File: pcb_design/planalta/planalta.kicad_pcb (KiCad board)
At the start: 2 copper layers, 93 x 93 mm, 158 parts, among them J1 USB_C_Receptacle, J2 USB_C_Receptacle, J3 USB_C_Receptacle, J4 USB_C_Receptacle, J5 Conn_02x13_Odd_Even, J6 Conn_02x03_Counter_Clockwise, J9 Conn_01x06_Female, Q1 Q_NMOS_GSD, Q2 Q_NMOS_GSD, Q3 Q_NMOS_GSD, Q4 Q_NMOS_GSD, Q5 Q_NMOS_GSD, SW1 SW_Push, U1 MAX4475_var, U10 dsPIC33EP512MC806, U11 DG2034E, U12 LP2985-5.0, U13 REF2033, U14 OPA320, U15 PGA113, U16 PGA113, U17 TPS737, U18 SiP32431, U19 SiP32431, U2 MAX4475_var, U20 SiP32431, U21 DG2034E, U22 DG2034E, U23 DG2034E, U24 SiP32431, U25 SiP32431, U3 MAX4475_var, U4 MAX4475_var, U5 PGA113, U6 PGA113, U7 MCP2542FD, U8 ADM7170, U9 ADS8332, Y1 Crystal_GND24

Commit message: Update.
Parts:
- moved D1 103.6 mm to (56.3, 129.4), turned to 90 degrees
- moved R17 98.4 mm to (56.3, 126.2), turned to 90 degrees
- moved D2 85.9 mm to (113.7, 129.4), turned to 90 degrees
- moved R18 79.6 mm to (113.7, 126.3), turned to 90 degrees
- moved C3 10.6 mm to (99.4, 48.4)
- moved R4 10.0 mm to (96.3, 48.4)
- moved Q3 9.94 mm to (92.7, 49.3)
- moved C36 9.09 mm to (58.7, 64.6)
- moved U18 9.09 mm to (58.7, 67.1)
- moved U7 8.74 mm to (92.3, 54.9)
- moved R3 7.16 mm to (95.9, 50.8), turned to -90 degrees
- moved C29 4.73 mm to (113.4, 80.6), turned to 0 degrees
- moved C20 3.37 mm to (100.0, 60.4)
- moved C19 3.30 mm to (97.5, 61.0)
- moved R33 3.13 mm to (89.2, 48.3), turned to 0 degrees
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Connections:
- net +3V3 renamed +3.3V
- J1 pad A10: /VMID -> /SCL1
- J1 pad A11: /CIN1 -> unconnected-(J1-PadA11)
- J1 pad A3: /OUT1 -> /SDA1
- J1 pad A6: /SDA1 -> /OUT1
- J1 pad A7: /SCL1 -> /CIN1
- J1 pad A8: unconnected-(J1-PadA8) -> /VMID
- J1 pad B10: /VMID -> /SCL1
- J1 pad B11: /CIN1 -> unconnected-(J1-PadB11)
- J1 pad B3: /OUT1 -> /SDA1
- J1 pad B6: /SDA1 -> /OUT1
- J1 pad B7: /SCL1 -> /CIN1
- J1 pad B8: unconnected-(J1-PadB8) -> /VMID
- J2 pad A10: /VMID -> /SCL1
- J2 pad A11: /CIN2 -> unconnected-(J2-PadA11)
- J2 pad A3: /OUT2 -> /SDA1
- J2 pad A6: /SDA1 -> /OUT2
- J2 pad A7: /SCL1 -> /CIN2
- J2 pad A8: unconnected-(J2-PadA8) -> /VMID
- J2 pad B10: /VMID -> /SCL1
- J2 pad B11: /CIN2 -> unconnected-(J2-PadB11)
- J2 pad B3: /OUT2 -> /SDA1
- J2 pad B6: /SDA1 -> /OUT2
- J2 pad B7: /SCL1 -> /CIN2
- J2 pad B8: unconnected-(J2-PadB8) -> /VMID
- J3 pad A10: /VMID -> /SCL2
- J3 pad A11: /CIN3 -> unconnected-(J3-PadA11)
- J3 pad A3: /OUT3 -> /SDA2
- J3 pad A6: /SDA2 -> /OUT3
- J3 pad A7: /SCL2 -> /CIN3
- J3 pad A8: unconnected-(J3-PadA8) -> /VMID
- J3 pad B10: /VMID -> /SCL2
- J3 pad B11: /CIN3 -> unconnected-(J3-PadB11)
- J3 pad B3: /OUT3 -> /SDA2
- J3 pad B6: /SDA2 -> /OUT3
- J3 pad B7: /SCL2 -> /CIN3
- J3 pad B8: unconnected-(J3-PadB8) -> /VMID
- J4 pad A10: /VMID -> /SCL2
- J4 pad A11: /CIN4 -> unconnected-(J4-PadA11)
- J4 pad A3: /OUT4 -> /SDA2
- J4 pad A6: /SDA2 -> /OUT4
- J4 pad A7: /SCL2 -> /CIN4
- J4 pad A8: unconnected-(J4-PadA8) -> /VMID
- J4 pad B10: /VMID -> /SCL2
- J4 pad B11: /CIN4 -> unconnected-(J4-PadB11)
- J4 pad B3: /OUT4 -> /SDA2
- J4 pad B6: /SDA2 -> /OUT4
- J4 pad B7: /SCL2 -> /CIN4
- J4 pad B8: unconnected-(J4-PadB8) -> /VMID
- J9 pad 6: /PGM -> unconnected-(J9-Pad6)
- U10 pad 28: unconnected-(U10-Pad28) -> /EN_VA
- U10 pad 55: unconnected-(U10-Pad55) -> /TERM
- U10 pad 58: /REF_C2 -> /C1RX
- U10 pad 60: /TERM -> /C1TX
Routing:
- net /BLK: track 33.7 -> 94.5 mm, vias 4 -> 6
- net /VMID: track 205.5 -> 173.5 mm, vias 17 -> 19
- net /SCL1: track 107.3 -> 137.7 mm, vias 4 -> 9
- net /SCL2: track 129.8 -> 156.0 mm, vias 8 -> 10
- net /EN_VA: track 0.00 -> 25.5 mm, vias 0 -> 2
- net GND: track 105.2 -> 83.3 mm, vias 61 -> 85
- net VBUS: track 431.0 -> 448.1 mm, vias 28 -> 27
- net /CIN2: track 44.5 -> 27.6 mm, vias 4 -> 2
- net /CIN1: track 44.0 -> 29.6 mm, vias 3 -> 2
- net /TERM: track 14.4 -> 28.7 mm, vias 0 -> 4
- net /CIN3: track 44.4 -> 30.5 mm, vias 2 -> 0
- net /SDA2: track 137.6 -> 150.8 mm, vias 9 -> 7
- net /C1TX: track 0.00 -> 11.6 mm
- net /C1RX: track 0.00 -> 10.4 mm
- net +4V: track 134.2 -> 143.9 mm
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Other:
- board text added: "GND ~{CTS} RX TX ~{RTS} 3V3"
- board text added: "Gloxinia plantalta rev. 7"
- board text added: "PWR"
- board text added: "STATUS"

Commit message: New and updated board designs.
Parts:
- removed J6: Conn_02x03_Counter_Clockwise, Connector_PinSocket_2.54mm:PinSocket_2x03_P2.54mm_Vertical
- J5: value Conn_02x13_Odd_Even -> Conn_02x07_Odd_Even; footprint Connector_PinHeader_2.54mm:PinHeader_2x13_P2.54mm_Vertical -> samtec:SAMTEC_TMMH-107-01-T-DV; moved to B.Cu
- N1: footprint custom_footprints:Enclosure-Gloxinia2 -> custom_footprints:Enclosure-Gloxinia4
- moved J5 12.0 mm to (85.0, 45.0), turned to 180 degrees
- moved R33 1.85 mm to (89.1, 50.1)
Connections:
- J5 pad 10: unconnected-(J5-Pad10) -> +3.3V
- J5 pad 11: /CAN_L -> GND
- J5 pad 12: unconnected-(J5-Pad12) -> GND
- J5 pad 13: unconnected-(J5-Pad13) -> GND
- J5 pad 14: unconnected-(J5-Pad14) -> GND
- J5 pad 2: VBUS -> /~{RTS}
- J5 pad 3: /V_USBC -> /CAN_H
- J5 pad 4: VBUS -> /~{CTS}
- J5 pad 5: /CAN_H -> /CAN_L
- J5 pad 6: /V_USBC -> /TX
- J5 pad 7: /CAN_H -> /CAN_C1
- J5 pad 8: unconnected-(J5-Pad8) -> /RX
- J5 pad 9: /CAN_L -> /CAN_C2
- U10 pad 21: unconnected-(U10-Pad21) -> /CAN_C2
- U10 pad 22: unconnected-(U10-Pad22) -> /CAN_C1
- U10 pad 49: /RX -> /~{RTS}
- U10 pad 50: /~{RTS} -> /~{CTS}
- U10 pad 51: /~{CTS} -> /TX
- U10 pad 52: /TX -> /RX
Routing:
- net /CAN_C2: track 0.00 -> 39.0 mm, vias 0 -> 1
- net /CAN_C1: track 0.00 -> 38.5 mm, vias 0 -> 1
- net +3.3V: track 370.8 -> 399.0 mm, vias 23 -> 25
- net /TX: track 17.9 -> 43.4 mm, vias 0 -> 1
- net /RX: track 19.1 -> 44.6 mm, vias 0 -> 1
- net /~{RTS}: track 16.4 -> 39.0 mm, vias 0 -> 1
- net /~{CTS}: track 20.2 -> 39.8 mm, vias 0 -> 1
- net /CAN_H: track 18.9 -> 9.11 mm, vias 2 -> 1
- net VBUS: track 448.1 -> 438.3 mm, vias 27 -> 31
- net /CAN_L: track 17.4 -> 13.4 mm, vias 0 -> 1
- net /V_USBC: track 3.59 -> 0.00 mm
- net /SYNC: track 2.54 -> 0.00 mm
- net Net-(C3-Pad1): track 9.20 -> 11.1 mm
- net /~{SD1}: track 95.4 -> 94.6 mm
- net /DRV1: track 53.2 -> 52.4 mm
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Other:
- outline, holes or cut-outs redrawn
- board text added: "Gloxinia plantalta rev. 8"
- board text removed: "Gloxinia plantalta rev. 7"

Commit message: Gerber exports
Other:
- rule pad_to_mask_clearance: 0.051 -> 0
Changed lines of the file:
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@@
       (dielectric_constraints no)
     )
-    (pad_to_mask_clearance 0.051)
-    (solder_mask_min_width 0.25)
+    (pad_to_mask_clearance 0)
     (pcbplotparams
       (layerselection 0x00010fc_ffffffff)
@@
       (drillshape 0)
       (scaleselection 1)
-      (outputdirectory "gerber")
+      (outputdirectory "gerber-planalta")
     )
   )

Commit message: Expose RTCC pin for synchronisation
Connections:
- J5 pad 10: +3.3V -> /RTCC
- J5 pad 12: GND -> +3.3V
- U10 pad 42: unconnected-(U10-Pad42) -> /RTCC
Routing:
- net /RTCC: track 0.00 -> 42.8 mm, vias 0 -> 3
- net +3.3V: track 399.0 -> 397.7 mm
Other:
- board text added: "Gloxinia plantalta rev. 9"
- board text removed: "Gloxinia plantalta rev. 8"
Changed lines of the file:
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@@
   (net 109 "unconnected-(U10-Pad27)")
   (net 110 "unconnected-(U10-Pad30)")
-  (net 111 "unconnected-(U10-Pad42)")
+  (net 111 "/RTCC")
   (net 112 "unconnected-(U10-Pad43)")
   (net 113 "+3.3V")
@@
       (net 2 "GND") (pinfunction "VSS") (pintype "power_in"))
     (pad "42" smd roundrect (at 5.6625 -0.75) (size 1.475 0.3) (layers "F.Cu" "F.Paste" "F.Mask") (roundrect_rratio 0.25)
-      (net 111 "unconnected-(U10-Pad42)") (pinfunction "RTCC/RPI72/RD8") (pintype "bidirectional+no_connect"))
+      (net 111 "/RTCC") (pinfunction "RTCC/RPI72/RD8") (pintype "bidirectional"))
     (pad "43" smd roundrect (at 5.6625 -1.25) (size 1.475 0.3) (layers "F.Cu" "F.Paste" "F.Mask") (roundrect_rratio 0.25)
       (net 112 "unconnected-(U10-Pad43)") (pinfunction "ASDA1/RPI73/RD9") (pintype "bidirectional+no_connect"))
@@
       (net 147 "/CAN_C2") (pinfunction "Pin_9") (pintype "passive"))
     (pad "10" smd rect (at 2 2.134 180) (size 1.016 3.3) (layers "B.Cu" "B.Paste" "B.Mask")
-      (net 113 "+3.3V") (pinfunction "Pin_10") (pintype "passive"))
+      (net 111 "/RTCC") (pinfunction "Pin_10") (pintype "passive"))
     (pad "11" smd rect (at 4 -2.135 180) (size 1.016 3.3) (layers "B.Cu" "B.Paste" "B.Mask")
       (net 2 "GND") (pinfunction "Pin_11") (pintype "passive"))
     (pad "12" smd rect (at 4 2.134 180) (size 1.016 3.3) (layers "B.Cu" "B.Paste" "B.Mask")
-      (net 2 "GND") (pinfunction "Pin_12") (pintype "passive"))
+      (net 113 "+3.3V") (pinfunction "Pin_12") (pintype "passive"))
     (pad "13" smd rect (at 6 -2.135 180) (size 1.016 3.3) (layers "B.Cu" "B.Paste" "B.Mask")
       (net 2 "GND") (pinfunction "Pin_13") (pintype "passive"))
@@
   (gr_line (start 38.5 38.5) (end 38.5 131.5) (layer "Edge.Cuts") (width 0.15))
   (gr_line (start 131.5 131.5) (end 38.5 131.5) (layer "Edge.Cuts") (width 0.15))
-  (gr_text "Gloxinia\nplantalta\nrev. 8" (at 57.275 43.45) (layer "F.SilkS")
+  (gr_text "Gloxinia\nplantalta\nrev. 9" (at 57.275 43.45) (layer "F.SilkS")
     (effects (font (size 1.5 1.5) (thickness 0.3)) (justify left))
   )
@@
   (segment (start 60.0005 74.25) (end 62.05 74.25) (width 0.3) (layer "B.Cu") (net 106))
   (segment (start 73.35 74.25) (end 81.2 74.25) (width 0.3) (layer "B.Cu") (net 106))
+  (segment (start 85.9 57) (end 82.1 53.2) (width 0.3) (layer "F.Cu") (net 111))
+  (segment (start 100.3 72.1) (end 99.9 71.7) (width 0.3) (layer "F.Cu") (net 111))
+  (segment (start 99.9 71.7) (end 99.1 71.7) (width 0.3) (layer "F.Cu") (net 111))
+  (segment (start 82.1 53.2) (end 82.1 52.55) (width 0.3) (layer "F.Cu") (net 111))
+  (segment (start 99.1 71.7) (end 96.45 71.7) (width 0.3) (layer "F.Cu") (net 111))
+  (segment (start 96.45 71.7) (end 95.65 70.9) (width 0.3) (layer "F.Cu") (net 111))
+  (segment (start 100.45 72.25) (end 100.3 72.1) (width 0.3) (layer "F.Cu") (net 111))
+  (segment (start 101.6625 72.25) (end 100.45 72.25) (width 0.3) (layer "F.Cu") (net 111))
+  (via (at 82.1 52.55) (size 0.8) (drill 0.4) (layers "F.Cu" "B.Cu") (net 111))
+  (via (at 85.9 57) (size 0.8) (drill 0.4) (layers "F.Cu" "B.Cu") (net 111))
+  (via (at 95.65 70.9) (size 0.8) (drill 0.4) (layers "F.Cu" "B.Cu") (net 111))
+  (segment (start 89.8 67.45) (end 89.15 66.8) (width 0.3) (layer "B.Cu") (net 111))
+  (segment (start 82.1 52.55) (end 82.1 43.766) (width 0.3) (layer "B.Cu") (net 111))
+  (segment (start 93.572792 67.45) (end 89.8 67.45) (width 0.3) (layer "B.Cu") (net 111))
+  (segment (start 82.1 43.766) (end 83 42.866) (width 0.3) (layer "B.Cu") (net 111))
+  (segment (start 89.15 60.3) (end 89.15 60.25) (width 0.3) (layer "B.Cu") (net 111))
+  (segment (start 89.15 66.8) (end 89.15 60.3) (width 0.3) (layer "B.Cu") (net 111))
+  (segment (start 89.15 60.25) (end 85.9 57) (width 0.3) (layer "B.Cu") (net 111))
+  (segment (start 95.65 69.527208) (end 93.572792 67.45) (width 0.3) (layer "B.Cu") (net 111))
+  (segment (start 95.65 70.9) (end 95.65 69.527208) (width 0.3) (layer "B.Cu") (net 111))
   (segment (start 73.3 100.05) (end 74.5125 100.05) (width 0.3) (layer "F.Cu") (net 113))
   (segment (start 47.25 62.4) (end 47.25 69.25) (width 0.5) (layer "F.Cu") (net 113))
@@
   (segment (start 73.3 100.05) (end 81.85 100.05) (width 0.5) (layer "B.Cu") (net 113))
   (segment (start 92.649511 100.699511) (end 92.65 100.7) (width 0.5) (layer "B.Cu") (net 113))
-  (segment (start 77.35 40) (end 82.3 40) (width 1) (layer "B.Cu") (net 113))
   (segment (start 102 56.1) (end 103.6 54.5) (width 0.5) (layer "B.Cu") (net 113))
-  (segment (start 83 40.7) (end 83 42.0664) (width 1) (layer "B.Cu") (net 113))
   (segment (start 76.2 41.15) (end 77.35 40) (width 1) (layer "B.Cu") (net 113))
   (segment (start 63.3 91.15) (end 57.75 91.15) (width 0.5) (layer "B.Cu") (net 113))
   (segment (start 103.6 54.5) (end 105.25 54.5) (width 0.5) (layer "B.Cu") (net 113))
+  (segment (start 77.35 40) (end 78.85 40) (width 1) (layer "B.Cu") (net 113))
   (segment (start 81.85 100.05) (end 83.45 100.05) (width 0.5) (layer "B.Cu") (net 113))
   (segment (start 64.75 100.05) (end 73.3 100.05) (width 0.3) (layer "B.Cu") (net 113))
@@
   (segment (start 106.35 98.630183) (end 104.767683 100.2125) (width 0.5) (layer "B.Cu") (net 113))
   (segment (start 104.767683 100.2125) (end 95.1125 100.2125) (width 0.5) (layer "B.Cu") (net 113))
+  (segment (start 81 40.9) (end 81 42.866) (width 1) (layer "B.Cu") (net 113))
   (segment (start 87.4875 68.5875) (end 88.15 69.25) (width 0.5) (layer "B.Cu") (net 113))
   (segment (start 94.8 53.9) (end 97 56.1) (width 0.5) (layer "B.Cu") (net 113))
-  (segment (start 82.3 40) (end 83 40.7) (width 1) (layer "B.Cu") (net 113))
+  (segment (start 78.85 40) (end 80.1 40) (width 1) (layer "B.Cu") (net 113))
   (segment (start 42.950489 72.299031) (end 44.14952 71.1) (width 0.5) (layer "B.Cu") (net 113))
   (segment (start 83.45 100.05) (end 84.099511 100.699511) (width 0.5) (layer "B.Cu") (net 113))
@@
   (segment (start 106.35 97.05) (end 106.35 98.630183) (width 0.5) (layer "B.Cu") (net 113))
   (segment (start 70.55 83.9) (end 73.2 83.9) (width 0.5) (layer "B.Cu") (net 113))
+  (segment (start 80.1 40) (end 81 40.9) (width 1) (layer "B.Cu") (net 113))
   (segment (start 120.20048 81.9) (end 120.20048 72.264763) (width 0.3) (layer "F.Cu") (net 114))
   (segment (start 120.70048 91.57452) (end 120.70048 82.4) (width 0.3) (layer "F.Cu") (net 114))

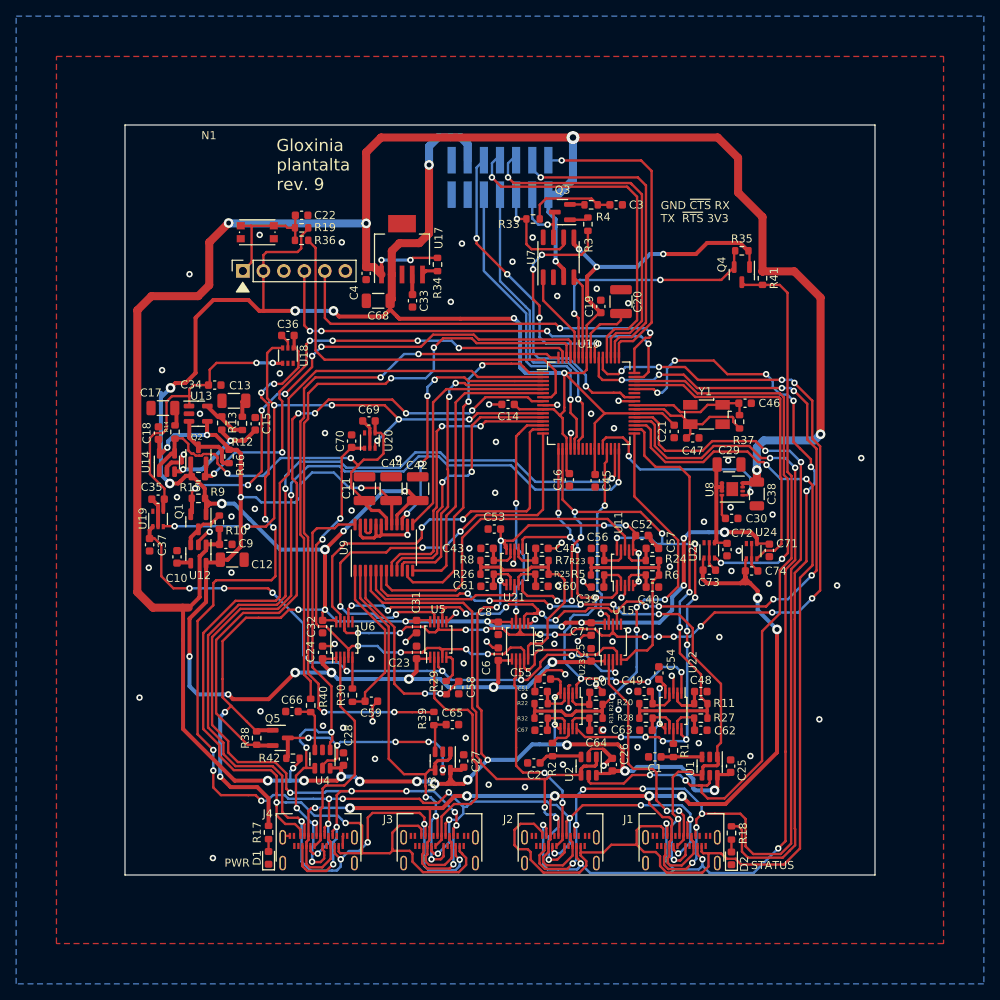
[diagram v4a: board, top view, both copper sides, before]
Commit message: Minor improvements.
Mostly related to external pull-ups of 10k for I2C
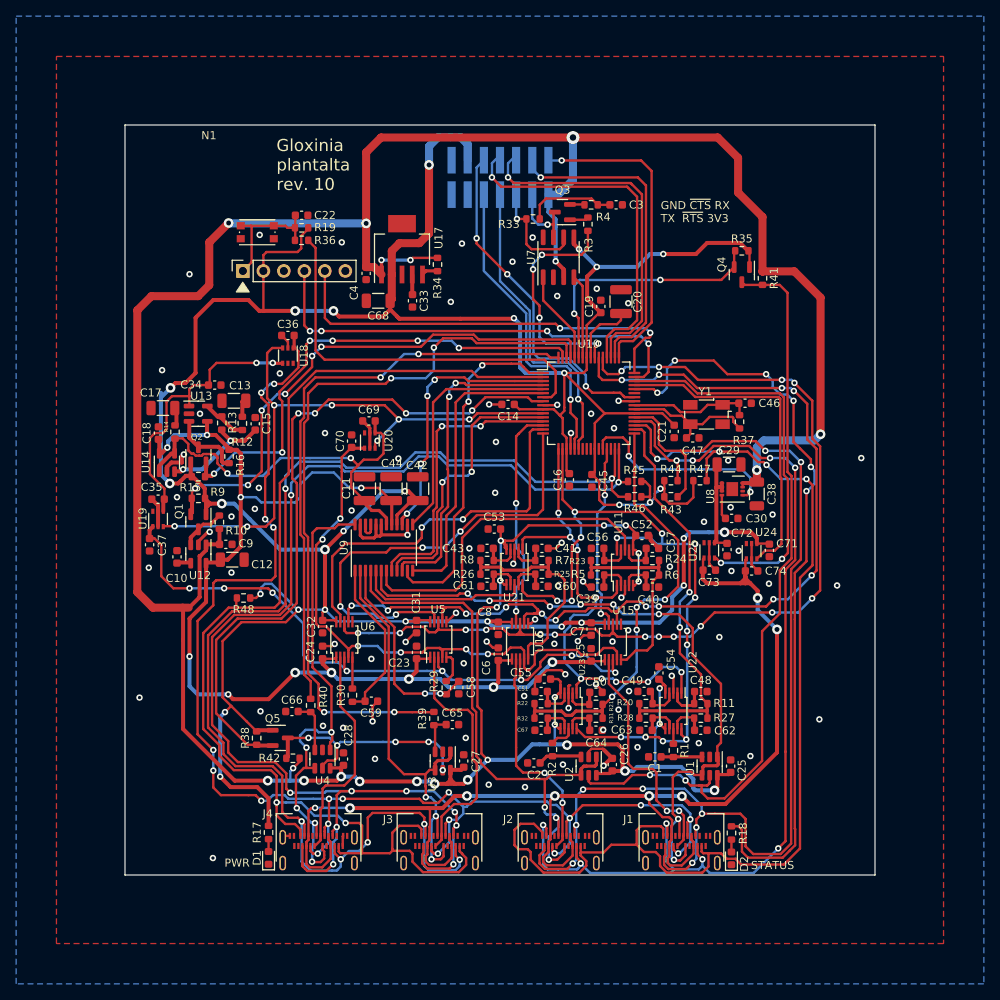
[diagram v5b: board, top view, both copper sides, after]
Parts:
- added R43: 10k, Resistor_SMD:R_0603_1608Metric, F.Cu at (106.2, 84.6)
- added R44: 10k, Resistor_SMD:R_0603_1608Metric, F.Cu at (106.2, 82.6)
- added R45: 10k, Resistor_SMD:R_0603_1608Metric, F.Cu at (101.7, 82.7)
- added R46: 10k, Resistor_SMD:R_0603_1608Metric, F.Cu at (101.7, 84.6)
- added R47: 10k, Resistor_SMD:R_0603_1608Metric, F.Cu at (109.8, 82.6)
- added R48: 10k, Resistor_SMD:R_0603_1608Metric, F.Cu at (53.2, 97.2)
- moved C45 0.40 mm to (96.4, 82.6)
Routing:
- net +3.3V: track 397.7 -> 432.1 mm, vias 25 -> 29
- net /SCL1: track 137.7 -> 144.0 mm
- net /~{INT1}: track 134.8 -> 139.5 mm, vias 2 -> 4
- net /SDA2: track 150.8 -> 155.1 mm
- net /SDA1: track 124.7 -> 127.6 mm, vias 7 -> 9
- net /SCL2: track 156.0 -> 157.8 mm
- net /DRV1: track 52.4 -> 50.7 mm
- net /~{INT2}: track 147.1 -> 148.7 mm
- net /~{SD2}_L: track 85.9 -> 86.5 mm
- net /DRV2: track 53.5 -> 54.0 mm
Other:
- board text added: "Gloxinia plantalta rev. 10"
- board text removed: "Gloxinia plantalta rev. 9"
